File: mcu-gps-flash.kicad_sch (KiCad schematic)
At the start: 32 parts, among them SW1 SW_Push, SW2 SW_Push, U12 ATGM336H-5N, U2 ESP32-C3-WROOM-02, U4 W25Q128JVS, U5 L96-M33, U6 L70-R

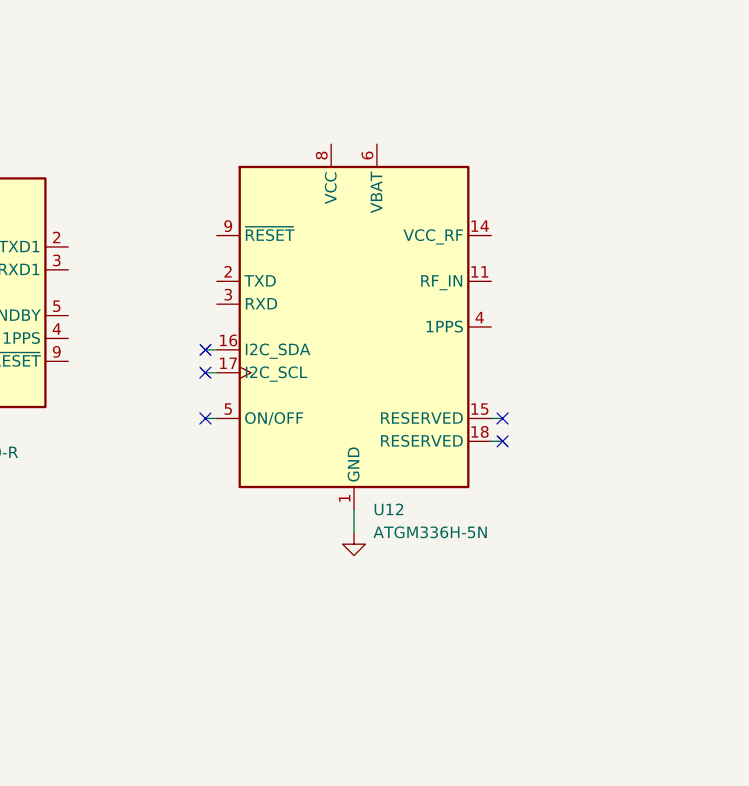
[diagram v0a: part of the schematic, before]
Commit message: Added ORing circuit for USB 5V and boost converter 5V
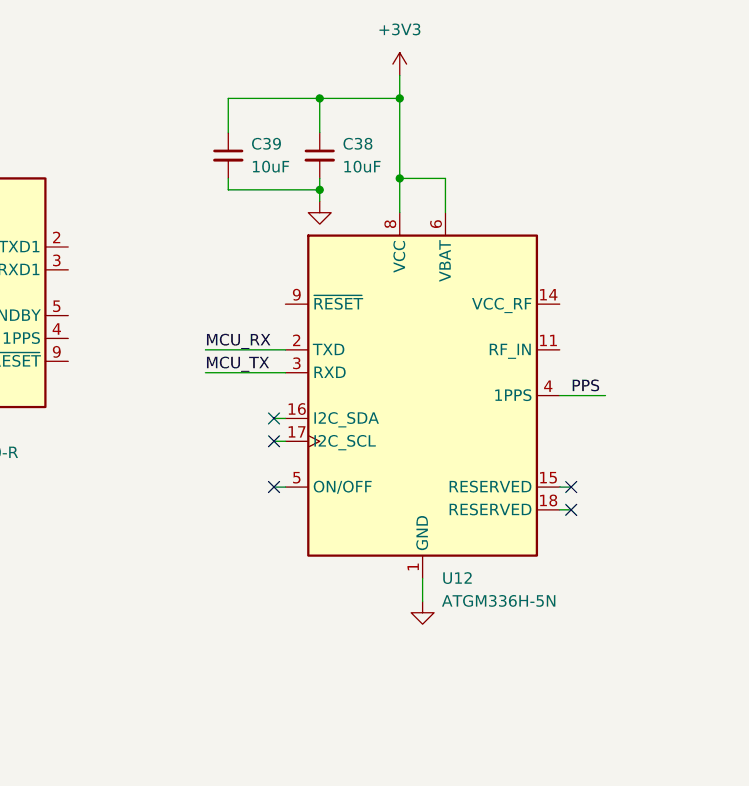
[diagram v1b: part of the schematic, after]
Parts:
- added C38, C39: 10uF, Capacitor_SMD:C_0603_1608Metric, symbol Device:C_Small
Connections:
- net +3V3: now also U12.6 (VBAT), U12.8 (VCC), C38.1, C39.1
- net GND: now also C38.2, C39.2
- net MCU_RX: now also U12.2 (TXD)
- net MCU_TX: now also U12.3 (RXD)
- net PPS: now also U12.4 (1PPS)
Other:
- moved on the sheet: U12
